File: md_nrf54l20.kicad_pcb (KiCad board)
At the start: 4 copper layers, 43.2 x 17.8 mm, 46 parts, among them J1 U.FL Conn, J10 Conn_01x15, J5 USB_C, J7 JST SH I2C, J9 Conn_01x15, SW1 RESET, U1 nRF54L20, U2 MCP1700x-280xxTT, U3 CH347T, U5 MLD-TF PUSH-H18, Y1 8MHz, Y2 32MHz

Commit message: Routing
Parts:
- removed C10: 10uF, Capacitor_SMD:C_0805_2012Metric
- removed J1: U.FL Conn, Connector_Coaxial:U.FL_Hirose_U.FL-R-SMT-1_Vertical
- removed U2: MCP1700x-280xxTT, Package_TO_SOT_SMD:SOT-23
- added C17: 1uF, Capacitor_SMD:C_0402_1005Metric, F.Cu at (97.5, 99.3)
- added C18: 1uF, Capacitor_SMD:C_0402_1005Metric, F.Cu at (112.4, 95.7)
- added J2: Conn_01x04, md-l20B:Chip Antenna AANI-CH-0070, F.Cu at (142.4, 89.9)
- added R4: 0, Resistor_SMD:R_0402_1005Metric, F.Cu at (139.0, 92.8)
- added R5: 0, Resistor_SMD:R_0402_1005Metric, F.Cu at (142.1, 92.8)
- added R7: 0, Resistor_SMD:R_0402_1005Metric, F.Cu at (140.5, 92.3)
- added U4: AP2112K-3.3, Package_TO_SOT_SMD:SOT-23-5, F.Cu at (110.1, 93.6)
- moved J7 27.1 mm to (122.4, 92.9), turned to -90 degrees
- moved SW1 23.9 mm to (122.6, 87.7)
- moved C9 16.5 mm to (97.0, 83.3)
- moved C11 14.5 mm to (97.4, 98.2)
- moved D4 12.2 mm to (125.5, 103.3)
- moved R12 12.2 mm to (125.5, 105.2)
- moved R1 5.98 mm to (137.5, 95.9)
- moved R8 4.60 mm to (127.2, 86.9)
- moved D3 4.60 mm to (127.2, 88.8)
- moved C16 4.55 mm to (136.4, 91.0)
- moved C2 4.55 mm to (128.7, 88.0)
- moved C5 4.55 mm to (133.5, 86.5)
- moved C6 4.55 mm to (129.9, 86.9)
- moved C7 4.55 mm to (136.4, 89.0)
- moved C8 4.55 mm to (135.4, 89.0)
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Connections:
- U1 pad 34: Net-(J1-In) -> /ANT
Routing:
- net /SWDCLK: track 2.05 -> 24.7 mm, vias 0 -> 2
- net /CH_UART_RX: track 1.47 -> 23.5 mm, vias 0 -> 2
- net /SWDIO: track 2.21 -> 23.0 mm, vias 0 -> 2
- net /D9_PWM: track 2.01 -> 18.9 mm
- net /D12_CITO: track 1.58 -> 16.9 mm
- net /D11_COTI: track 2.70 -> 16.8 mm
- net /D10_CS: track 3.65 -> 17.5 mm
- net /CH_UART_TX: track 3.44 -> 15.9 mm, vias 1 -> 2
- net Net-(J1-In): track 10.1 -> 0.00 mm
- net /SD_CS: track 0.00 -> 9.65 mm, vias 0 -> 1
- net /SD_MOSI: track 0.00 -> 9.49 mm, vias 0 -> 1
- net /A4_SDA: track 11.3 -> 2.14 mm, vias 1 -> 0
- net /A5_SCL: track 10.6 -> 1.42 mm, vias 1 -> 0
- net /SD_MISO: track 1.81 -> 9.88 mm, vias 0 -> 1
- net /A0: track 2.54 -> 10.3 mm, vias 1 -> 0
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
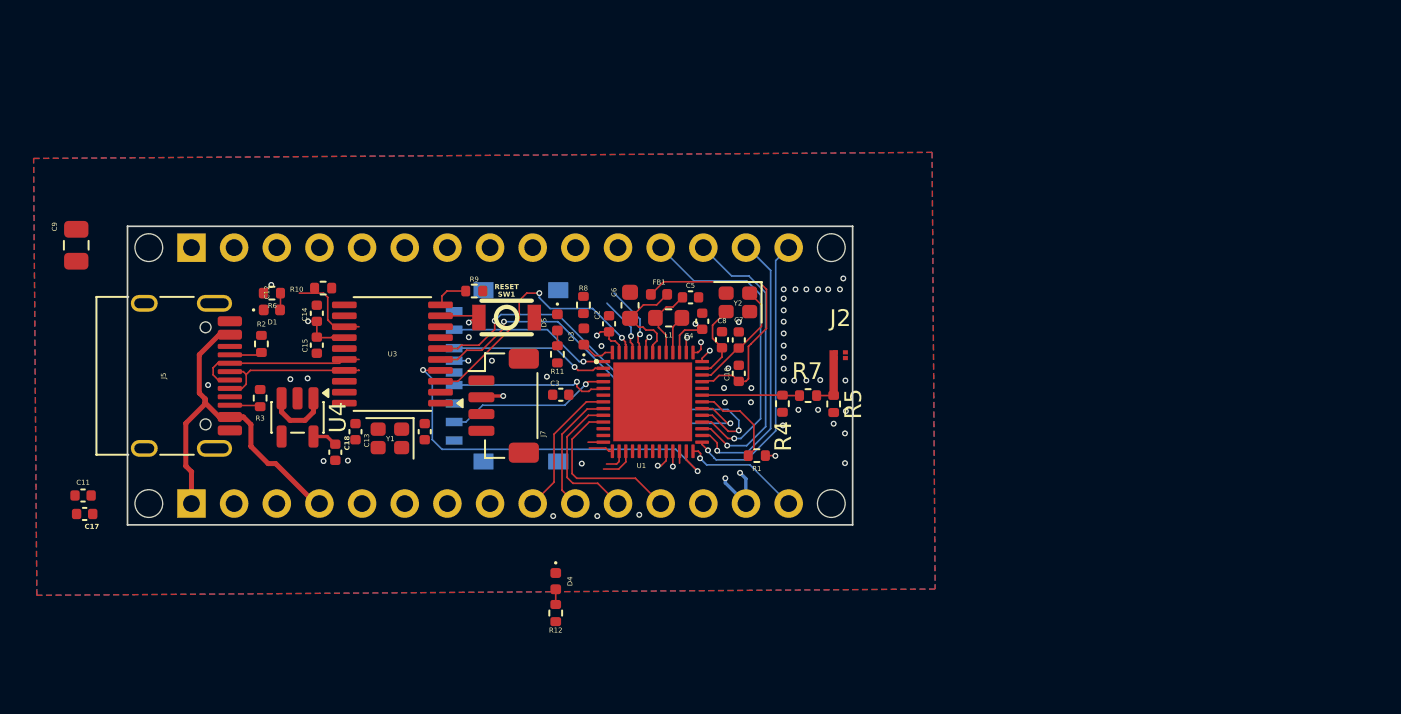
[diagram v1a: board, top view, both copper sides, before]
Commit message: Mirrored headers, swapping
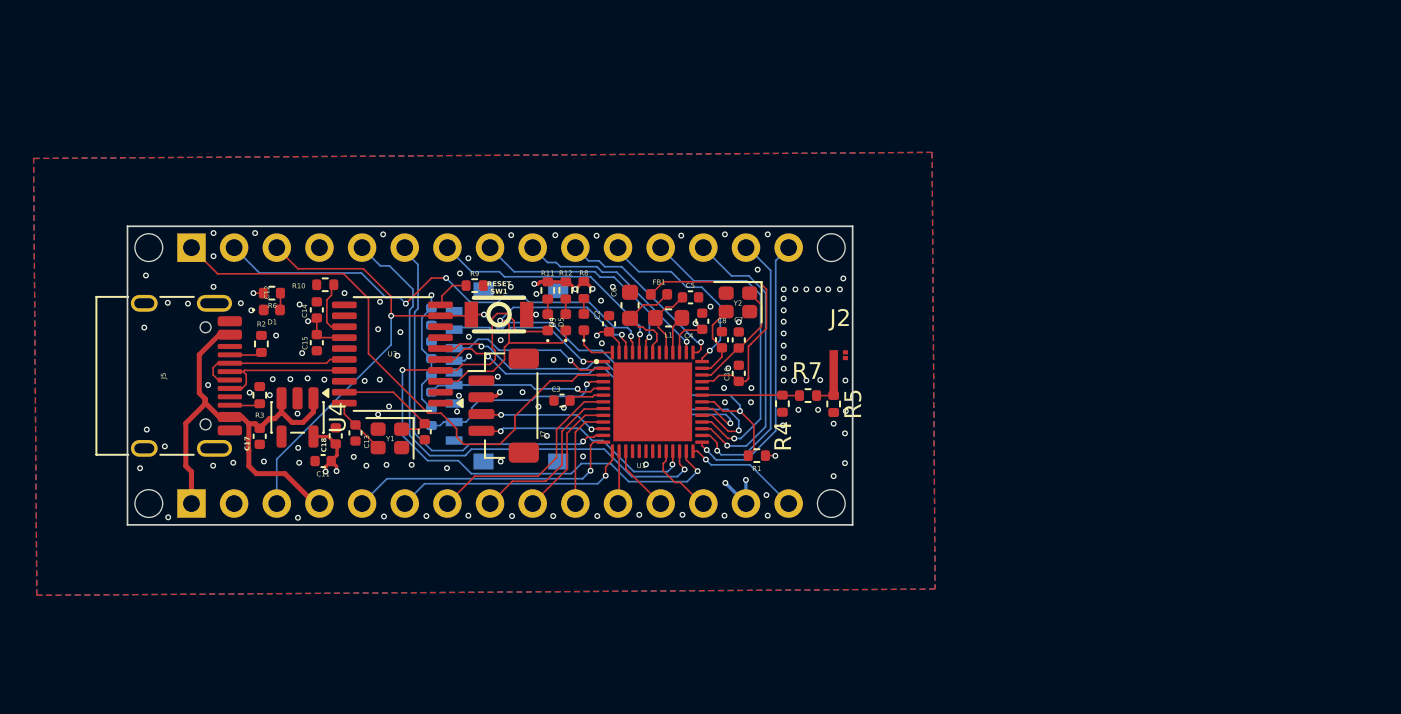
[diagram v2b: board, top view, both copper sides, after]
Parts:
- removed C9: 10uF, Capacitor_SMD:C_0805_2012Metric
- added R13: 10k, Resistor_SMD:R_0402_1005Metric, B.Cu at (118.1, 87.6)
- added R14: 10k, Resistor_SMD:R_0402_1005Metric, B.Cu at (118.1, 89.6)
- added R15: 10k, Resistor_SMD:R_0402_1005Metric, B.Cu at (118.1, 91.6)
- added R16: 10k, Resistor_SMD:R_0402_1005Metric, B.Cu at (118.1, 93.6)
- moved R12 19.2 mm to (126.1, 86.0), turned to 90 degrees
- moved D4 15.4 mm to (126.1, 87.9), turned to 90 degrees
- moved C11 14.4 mm to (111.7, 96.2), turned to 180 degrees
- moved C17 11.4 mm to (107.9, 94.7), turned to -90 degrees
- moved R11 3.85 mm to (125.0, 86.0), turned to 90 degrees
- moved C18 0.98 mm to (112.4, 94.7), turned to 90 degrees
- moved R8 0.90 mm to (127.2, 86.0)
- moved D3 0.86 mm to (127.2, 87.9)
- moved D5 0.58 mm to (125.0, 87.9), turned to 90 degrees
- moved SW1 0.48 mm to (122.1, 87.5)
- moved C3 0.36 mm to (125.9, 92.6)
- moved R9 0.33 mm to (120.7, 85.8)
- moved R10 0.24 mm to (111.8, 85.7)
- moved C14 0.20 mm to (111.3, 87.2)
- moved R3 0.18 mm to (107.9, 92.3)
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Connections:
- J9 pad 10: /A2 -> /A0
- J9 pad 11: /A1 -> /A5_SCL
- J9 pad 12: /A0 -> /A4_SDA
- J9 pad 13: unconnected-(J9-Pin_13-Pad13) -> /EXTREF
- J9 pad 5: unconnected-(J9-Pin_5-Pad5) -> /A7
- J9 pad 6: unconnected-(J9-Pin_6-Pad6) -> /A6
- J9 pad 7: /A5_SCL -> /A3
- J9 pad 8: /A4_SDA -> /A2
- J9 pad 9: /A3 -> /A1
- U1 pad 1: /SD_CS -> /SD_SCK
- U1 pad 11: unconnected-(U1-P1.01-Pad11) -> /QWIIC_SDA
- U1 pad 12: unconnected-(U1-P1.02-Pad12) -> /D3_PWM
- U1 pad 13: /D8 -> /A7
- U1 pad 14: /D7 -> /A5_SCL
- U1 pad 15: /A5_SCL -> /A6
- U1 pad 22: /D6_PWM -> /EXTREF
- U1 pad 23: /D5_PWM -> /QWIIC_SCL
- U1 pad 24: /D4 -> /D2
- U1 pad 3: unconnected-(U1-P2.03-Pad3) -> /D4
- U1 pad 30: /D9_PWM -> /CH_UART_TX
- U1 pad 39: /D3_PWM -> /D8
- U1 pad 40: /D2 -> /D7
- U1 pad 41: /D1_TX -> /D6_PWM
- U1 pad 47: /D0_RX -> /D5_PWM
- U1 pad 48: /QWIIC_SDA -> /D1_TX
- U1 pad 49: /QWIIC_SCL -> /D0_RX
- U1 pad 5: /SD_SCK -> /SD_CS
- U1 pad 50: /CH_UART_TX -> /D9_PWM
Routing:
- net /nRESET: track 8.32 -> 52.6 mm, vias 1 -> 3
- net /D1_TX: track 0.91 -> 33.7 mm, vias 1 -> 0
- net /D2: track 0.98 -> 31.9 mm
- net /D0_RX: track 0.99 -> 28.7 mm, vias 1 -> 3
- net /D3_PWM: track 0.84 -> 23.5 mm
- net /A7: track 0.00 -> 16.8 mm, vias 0 -> 1
- net +3V3: track 17.3 -> 33.7 mm, vias 9 -> 16
- net /D4: track 0.71 -> 15.0 mm, vias 0 -> 1
- net /A6: track 0.00 -> 14.3 mm, vias 0 -> 1
- net /CH_UART_RX: track 23.5 -> 37.3 mm
- net /D5_PWM: track 0.91 -> 13.6 mm
- net /D6_PWM: track 1.18 -> 12.1 mm
- net /D8: track 0.91 -> 11.4 mm, vias 0 -> 1
- net /QWIIC_SCL: track 3.59 -> 13.6 mm, vias 1 -> 2
- net /D7: track 1.45 -> 10.8 mm, vias 0 -> 1
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
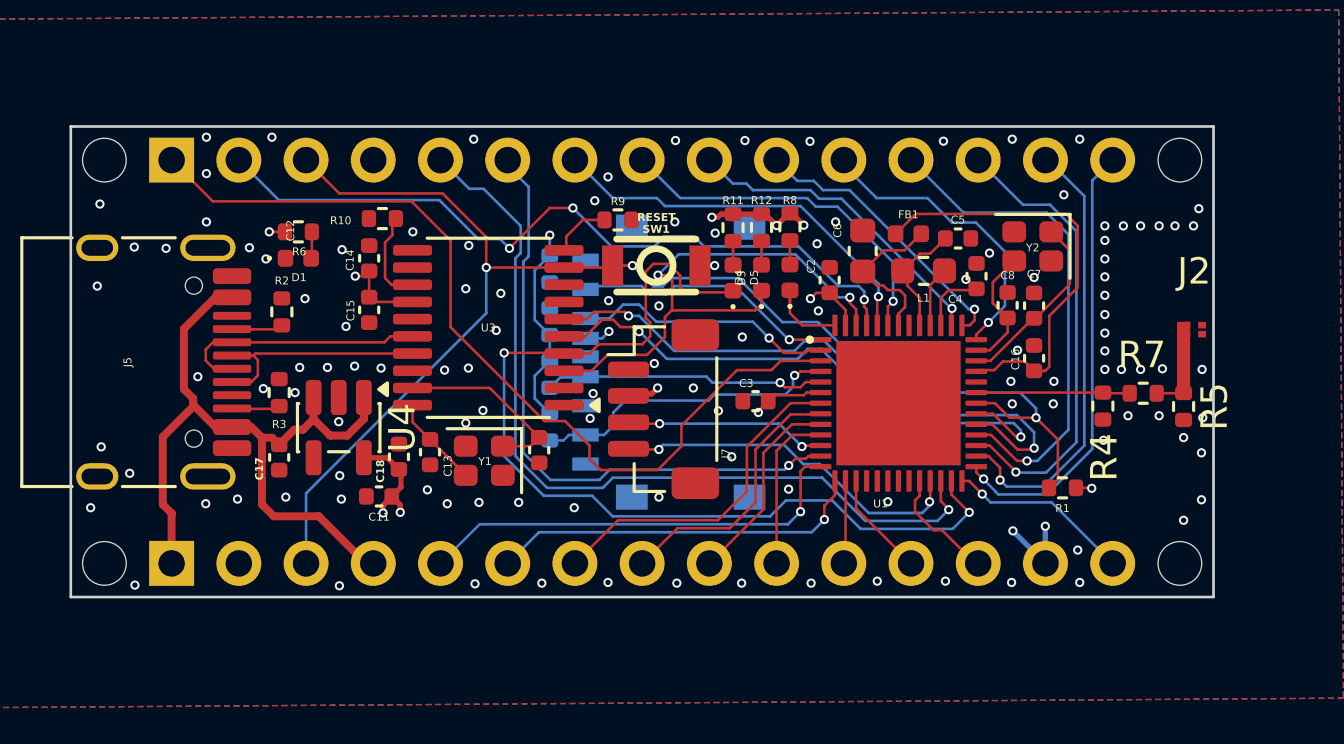
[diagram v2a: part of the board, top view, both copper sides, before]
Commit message: Analog header swap, start digital
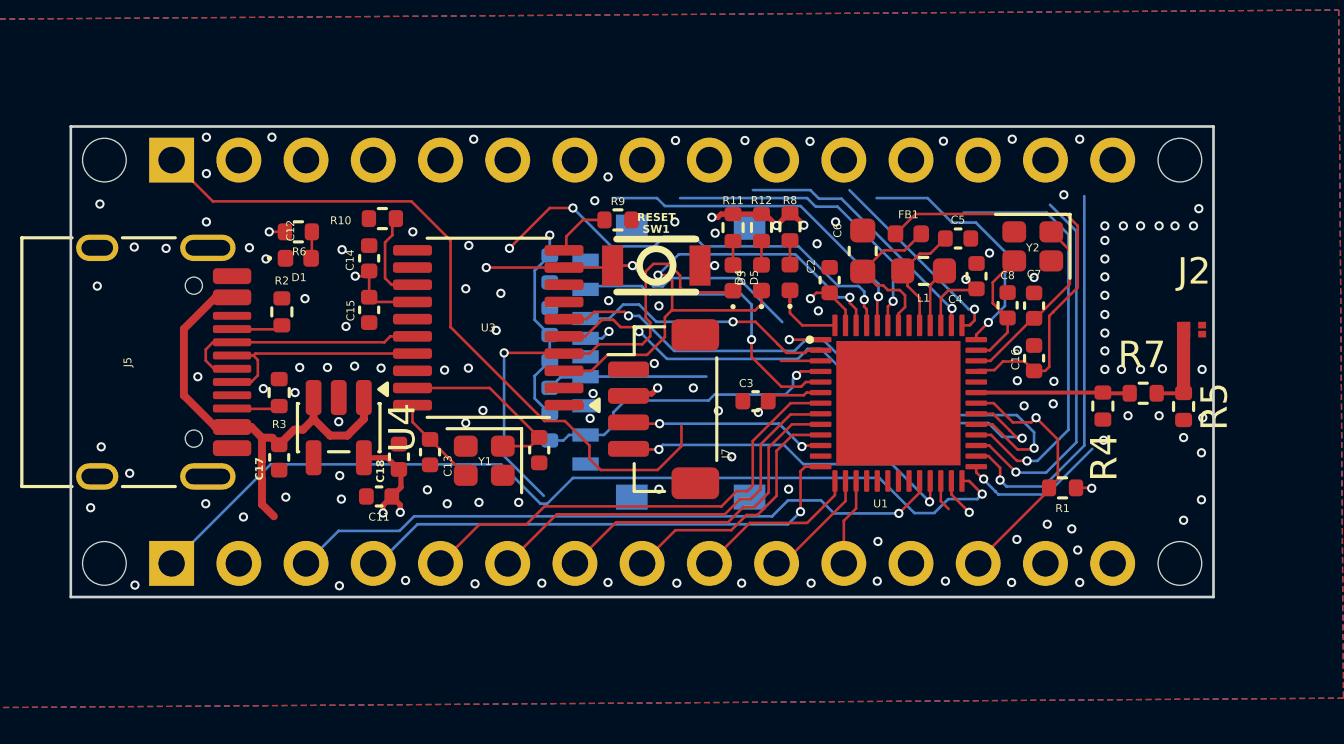
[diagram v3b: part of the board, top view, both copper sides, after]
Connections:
- J10 pad 1: /D1_TX -> /D12_CITO
- J10 pad 10: /D7 -> /D3_PWM
- J10 pad 11: /D8 -> /D2
- J10 pad 12: /D9_PWM -> GND
- J10 pad 13: /D10_CS -> /nRESET
- J10 pad 14: /D11_COTI -> /D0_RX
- J10 pad 15: /D12_CITO -> /D1_TX
- J10 pad 2: /D0_RX -> /D11_COTI
- J10 pad 3: /nRESET -> /D10_CS
- J10 pad 4: GND -> /D9_PWM
- J10 pad 5: /D2 -> /D8
- J10 pad 6: /D3_PWM -> /D7
- J10 pad 7: /D4 -> /D6_PWM
- J10 pad 9: /D6_PWM -> /D4
- J9 pad 1: VBUS -> /D13_SCK
- J9 pad 10: /A0 -> /A6
- J9 pad 11: /A5_SCL -> /A7
- J9 pad 12: /A4_SDA -> VBUS
- J9 pad 13: /EXTREF -> /nRESET
- J9 pad 14: +3V3 -> GND
- J9 pad 15: /D13_SCK -> VBUS
- J9 pad 2: GND -> +3V3
- J9 pad 3: /nRESET -> /EXTREF
- J9 pad 4: VBUS -> /A0
- J9 pad 5: /A7 -> /A1
- J9 pad 6: /A6 -> /A2
- J9 pad 8: /A2 -> /A4
- J9 pad 9: /A1 -> /A5_SCL
- U1 pad 10: /A0 -> /A4
- U1 pad 13: /A7 -> /A0
- U1 pad 16: /A4_SDA -> /A7
- U1 pad 7: /A3 -> /A1
- U1 pad 9: /A1 -> /A3
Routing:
- net /D2: track 31.9 -> 1.38 mm, vias 1 -> 0
- net /nRESET: track 52.6 -> 22.2 mm
- net /D13_SCK: track 6.99 -> 35.0 mm
- net /D3_PWM: track 23.5 -> 0.00 mm, vias 1 -> 0
- net /D1_TX: track 33.7 -> 13.0 mm, vias 0 -> 1
- net /EXTREF: track 4.43 -> 25.1 mm, vias 0 -> 1
- net /D9_PWM: track 18.9 -> 0.00 mm, vias 1 -> 0
- net /CH_UART_RX: track 37.3 -> 20.0 mm
- net /D12_CITO: track 16.9 -> 33.2 mm
- net /CH_UART_TX: track 20.6 -> 36.7 mm, vias 2 -> 3
- net /D4: track 15.0 -> 1.51 mm, vias 1 -> 0
- net /A7: track 16.8 -> 3.40 mm, vias 1 -> 0
- net /A0: track 6.77 -> 19.3 mm, vias 0 -> 1
- net /D0_RX: track 28.7 -> 17.2 mm
- net VBUS: track 29.8 -> 18.4 mm
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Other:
- board text removed: "ICSP"

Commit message: Fixing Digital mapping
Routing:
- net /D11_COTI: track 14.9 -> 5.47 mm
- net VBUS: track 18.4 -> 15.2 mm
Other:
- board text added: "<- Impedance match"
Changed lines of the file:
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@@
 		(layer "Edge.Cuts")
 	)
-	(gr_rect
-		(start 139.975 86.7)
-		(end 143.175 94.7)
-		(stroke
-			(width 0.1)
-			(type solid)
+	(gr_text "<- Impedance match"
+		(at 144.725 93.075 0)
+		(layer "F.SilkS")
+		(effects
+			(font
+				(size 1.5 1.5)
+				(thickness 0.3)
+				(bold yes)
+			)
+			(justify left bottom)
 		)
-		(fill no)
-		(layer "F.Fab")
 	)
 	(gr_text "USB-C\n"
@@
 	)
 	(via
-		(at 111.725 91.35)
+		(at 111.675 91.225)
 		(size 0.35)
 		(drill 0.2)
@@
 	)
 	(via
-		(at 110.725 91.275)
+		(at 110.725 91.225)
 		(size 0.35)
 		(drill 0.2)
@@
 	)
 	(via
-		(at 109.7 91.325)
+		(at 109.625 91.225)
 		(size 0.35)
 		(drill 0.2)
@@
 	)
 	(via
-		(at 108.65 91.325)
+		(at 108.7 91.225)
 		(size 0.35)
 		(drill 0.2)
@@
 	)
 	(segment
-		(start 138.298959 94.276777)
-		(end 138.298959 84.848959)
-		(width 0.1)
-		(layer "B.Cu")
-		(net "/D11_COTI")
-	)
-	(segment
 		(start 135.359027 95.825)
 		(end 136.750736 95.825)
@@
 	)
 	(segment
-		(start 107.610001 93.980001)
-		(end 107.875 94.245)
-		(width 0.3)
-		(layer "F.Cu")
-		(net "VBUS")
-	)
-	(segment
-		(start 106.819999 93.575)
-		(end 107.225 93.980001)
-		(width 0.3)
-		(layer "F.Cu")
-		(net "VBUS")
-	)
-	(segment
-		(start 107.225 93.980001)
-		(end 107.610001 93.980001)
-		(width 0.3)
-		(layer "F.Cu")
-		(net "VBUS")
-	)
-	(segment
-		(start 107.225 96.5)
-		(end 107.675 96.95)
+		(start 107.205 93.575)
+		(end 106.095 93.575)
 		(width 0.3)
 		(layer "F.Cu")
@@
 	)
 	(segment
-		(start 107.225 93.980001)
-		(end 107.225 94.848154)
-		(width 0.3)
-		(layer "F.Cu")
-		(net "VBUS")
-	)
-	(segment
 		(start 111.075 92.4625)
 		(end 111.075 92.744842)
@@
 	)
 	(segment
-		(start 107.225 94.848154)
-		(end 107.215 94.858154)
-		(width 0.3)
-		(layer "F.Cu")
-		(net "VBUS")
-	)
-	(segment
-		(start 106.095 93.575)
-		(end 106.819999 93.575)
-		(width 0.3)
-		(layer "F.Cu")
-		(net "VBUS")
-	)
-	(segment
 		(start 109.175 92.4625)
 		(end 109.175 93.275)
@@
 	)
 	(segment
-		(start 107.215 95.551846)
-		(end 107.225 95.561846)
-		(width 0.3)
-		(layer "F.Cu")
-		(net "VBUS")
-	)
-	(segment
 		(start 105.46688 93.575)
 		(end 104.275 92.38312)
@@
 	)
 	(segment
-		(start 107.215 94.858154)
-		(end 107.215 95.551846)
-		(width 0.3)
-		(layer "F.Cu")
-		(net "VBUS")
-	)
-	(segment
 		(start 105.46688 88.675)
 		(end 106.095 88.675)
@@
 	)
 	(segment
-		(start 107.225 95.561846)
-		(end 107.225 96.5)
+		(start 107.875 94.245)
+		(end 107.205 93.575)
 		(width 0.3)
 		(layer "F.Cu")

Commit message: Routing digital
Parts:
- added D6: G_LED, LED_SMD:LED_0402_1005Metric, F.Cu at (133.5, 73.1)
- added R17: 220, Resistor_SMD:R_0402_1005Metric, F.Cu at (128.1, 73.0)
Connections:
- J7 pad 3: /QWIIC_SDA -> /A4
- J7 pad 4: /QWIIC_SCL -> /A5_SCL
- U1 pad 11: /QWIIC_SDA -> unconnected-(U1-P1.01-Pad11)
- U1 pad 23: /QWIIC_SCL -> unconnected-(U1-P1.08-Pad23)
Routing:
- net /CH_UART_RX: track 20.0 -> 34.4 mm, vias 2 -> 3
- net /A5_SCL: track 6.35 -> 19.8 mm, vias 0 -> 2
- net /QWIIC_SCL: track 13.1 -> 0.00 mm, vias 2 -> 0
- net /D12_CITO: track 33.2 -> 20.8 mm
- net /D1_TX: track 13.0 -> 1.16 mm
- net /CH_UART_TX: track 36.7 -> 26.1 mm, vias 3 -> 2
- net /D10_CS: track 14.1 -> 4.87 mm
- net /QWIIC_SDA: track 7.61 -> 0.00 mm, vias 2 -> 0
- net /A4: track 9.75 -> 17.4 mm, vias 0 -> 2
- net /nRESET: track 22.2 -> 14.8 mm, vias 3 -> 2
- net /D8: track 9.46 -> 2.27 mm
- net /D0_RX: track 17.2 -> 14.3 mm, vias 3 -> 1
- net +3V3: track 30.6 -> 28.2 mm, vias 14 -> 11
- net /D13_SCK: track 35.0 -> 33.4 mm
- net /D2: track 1.38 -> 0.20 mm
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
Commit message: Swapping from ch347t to ch347f
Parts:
- added U6: CH347F, Package_DFN_QFN:QFN-28-1EP_4x4mm_P0.4mm_EP2.4x2.4mm, F.Cu at (117.0, 77.6)
